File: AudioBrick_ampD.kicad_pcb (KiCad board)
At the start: 2 copper layers, 70 x 70 mm, 5 parts, among them U1 TPA3251

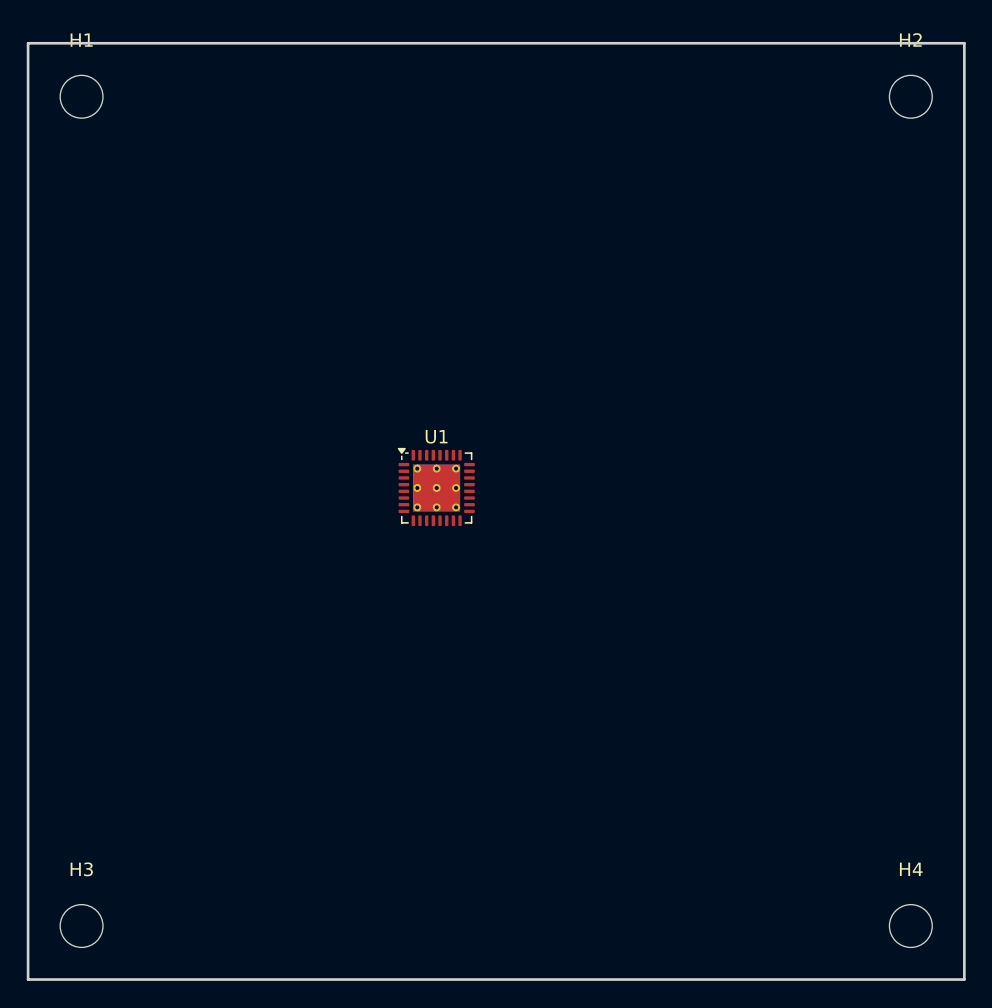
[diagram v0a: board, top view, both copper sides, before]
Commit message: output LC filter
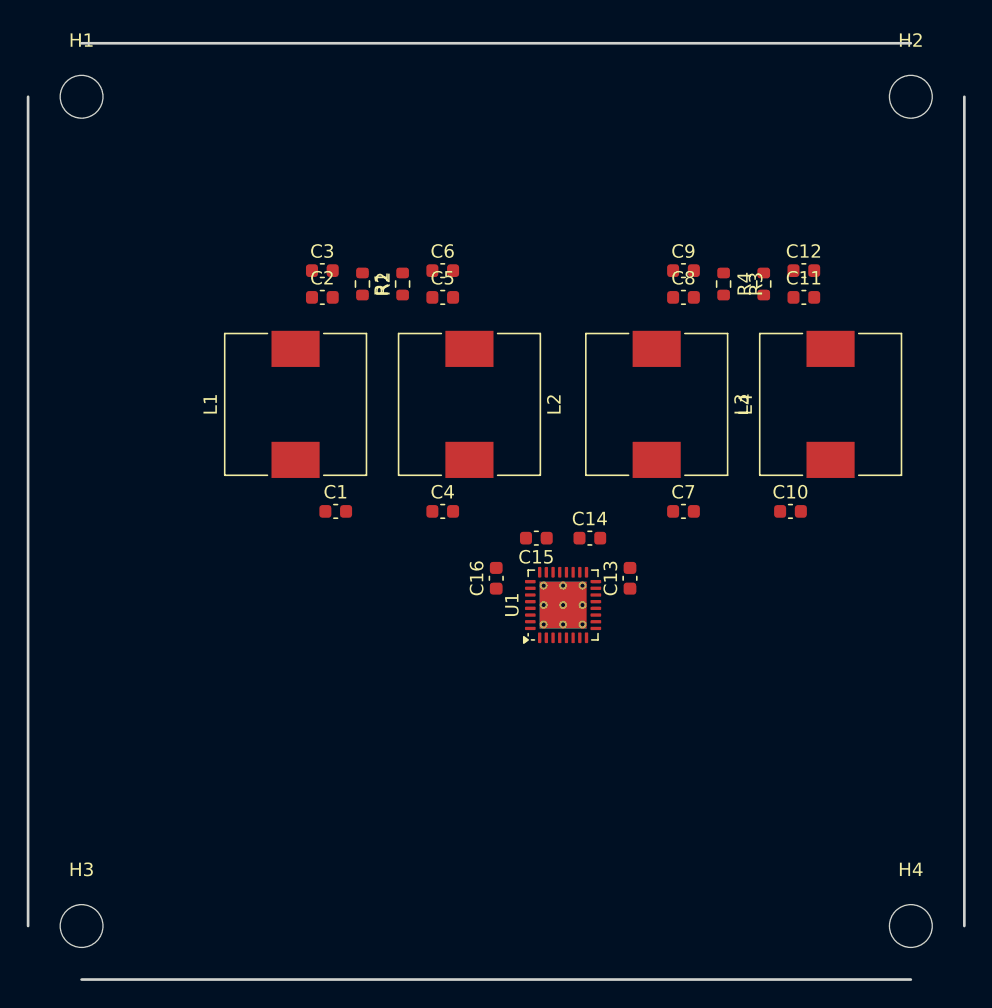
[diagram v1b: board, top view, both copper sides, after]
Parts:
- added C1: 680nF, Capacitor_SMD:C_0603_1608Metric, F.Cu at (143.0, 95.0)
- added C10: 680nF, Capacitor_SMD:C_0603_1608Metric, F.Cu at (177.0, 95.0)
- added C11: 1nF, Capacitor_SMD:C_0603_1608Metric, F.Cu at (178.0, 79.0)
- added C12: 10nF, Capacitor_SMD:C_0603_1608Metric, F.Cu at (178.0, 77.0)
- added C13: 220nF, Capacitor_SMD:C_0603_1608Metric, F.Cu at (165.0, 100.0)
- added C14: 220nF, Capacitor_SMD:C_0603_1608Metric, F.Cu at (162.0, 97.0)
- added C15: 220nF, Capacitor_SMD:C_0603_1608Metric, F.Cu at (158.0, 97.0)
- added C16: 220nF, Capacitor_SMD:C_0603_1608Metric, F.Cu at (155.0, 100.0)
- added C2: 1nF, Capacitor_SMD:C_0603_1608Metric, F.Cu at (142.0, 79.0)
- added C3: 10nF, Capacitor_SMD:C_0603_1608Metric, F.Cu at (142.0, 77.0)
- added C4: 680nF, Capacitor_SMD:C_0603_1608Metric, F.Cu at (151.0, 95.0)
- added C5: 1nF, Capacitor_SMD:C_0603_1608Metric, F.Cu at (151.0, 79.0)
- added C6: 10nF, Capacitor_SMD:C_0603_1608Metric, F.Cu at (151.0, 77.0)
- added C7: 680nF, Capacitor_SMD:C_0603_1608Metric, F.Cu at (169.0, 95.0)
- added C8: 1nF, Capacitor_SMD:C_0603_1608Metric, F.Cu at (169.0, 79.0)
- added C9: 10nF, Capacitor_SMD:C_0603_1608Metric, F.Cu at (169.0, 77.0)
- added L1: 10uH, Inductor_SMD:L_10.4x10.4_H4.8, F.Cu at (140.0, 87.0)
- added L2: 10uH, Inductor_SMD:L_10.4x10.4_H4.8, F.Cu at (153.0, 87.0)
- added L3: 10uH, Inductor_SMD:L_10.4x10.4_H4.8, F.Cu at (167.0, 87.0)
- added L4: 10uH, Inductor_SMD:L_10.4x10.4_H4.8, F.Cu at (180.0, 87.0)
- added R1: 3R3, Resistor_SMD:R_0603_1608Metric, F.Cu at (145.0, 78.0)
- added R2: 3R3, Resistor_SMD:R_0603_1608Metric, F.Cu at (148.0, 78.0)
- added R3: 3R3, Resistor_SMD:R_0603_1608Metric, F.Cu at (172.0, 78.0)
- added R4: 3R3, Resistor_SMD:R_0603_1608Metric, F.Cu at (175.0, 78.0)
- U1: value TPA3251 -> TPA313xD2
- moved U1 12.9 mm to (160.0, 102.0), turned to 90 degrees
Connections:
- U1 pad 15: unconnected-(U1A-BSPL-Pad15) -> Net-(U1-BSPL)
- U1 pad 16: unconnected-(U1A-OUTPL-Pad16) -> Net-(U1-OUTPL)
- U1 pad 18: unconnected-(U1A-OUTNL-Pad18) -> Net-(U1-OUTNL)
- U1 pad 19: unconnected-(U1A-BSNL-Pad19) -> Net-(U1-BSNL)
- U1 pad 22: unconnected-(U1A-BSNR-Pad22) -> Net-(U1-BSNR)
- U1 pad 23: unconnected-(U1A-OTNR-Pad23) -> Net-(U1-OTNR)
- U1 pad 25: unconnected-(U1A-OUTPR-Pad25) -> Net-(U1-OUTPR)
- U1 pad 26: unconnected-(U1A-BSPR-Pad26) -> Net-(U1-BSPR)
- U1 pad 33: (no net) -> unconnected-(U1-TP/GND-Pad33)
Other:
- outline, holes or cut-outs redrawn
